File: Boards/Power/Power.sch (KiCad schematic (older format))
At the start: 105 parts, among them IC1 PIC32MM0064GPM048, K1 Relay(Mech/SSR), K2 Relay(Mech/SSR), K3 Relay(Mech/SSR), K4 Relay(Mech/SSR), K5 Relay(Mech/SSR), K6 Relay(Mech/SSR), K7 Relay(Mech/SSR), K8 Relay(Mech/SSR), P1 Stab and 1x3, P10 1x6 2.54 Pin Header, P11 Stacked USBA, P12 1x2 5.08, P13 1x2 5.08, P2 Stab and 1x3, P3 Stab and 1x3, P4 Stab and 1x3, P5 Stab and 1x3, P6 Stab and 1x3, P7 Stab and 1x3, P8 Stab and 1x3, Q1 NX7002AK, Q10 NX7002AK, Q11 NX7002AK, Q2 NX7002AK, Q3 NX7002AK, Q4 NX7002AK, Q5 NX7002AK, Q6 NX7002AK, Q7 NX7002AK, Q8 NX7002AK, Q9 NX7002AK, U1 ST485EC, U2 AP2114H, U3 LTV-826, U4 LTV-826, X1 8MHz

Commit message: Power bom is now controlled by schematic
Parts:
- added N1: Housing, symbol Mechanical:Housing
- added P11, P12, P13, P14, P15, P16, P17, P18: Current, Connector_PinSocket_2.54mm:PinSocket_1x03_P2.54mm_Vertical, symbol Connector_Generic:Conn_01x03
- C1, C2, C3, C4: symbol C_Small -> Power-rescue:C_Small; Comments (none) -> 0805, 50V, X7R, 10%; Digi-Key Part Number (none) -> 445-7534-1-ND; Manufacturer (none) -> TDK; Manufacturer Part Number (none) -> C2012X7R1H104K085AA; Type (none) -> Capacitor
- C5: symbol C -> Power-rescue:C_Small; Comments (none) -> 0805, 50V, X7R, 10%; Digi-Key Part Number (none) -> 445-7534-1-ND; Manufacturer (none) -> TDK; Manufacturer Part Number (none) -> C2012X7R1H104K085AA; Type (none) -> Capacitor
- C6, C7: symbol C_Small -> Power-rescue:C_Small; Comments (none) -> 0805, 10V, X7R, 10%; Digi-Key Part Number (none) -> 1276-2972-1-ND; Manufacturer (none) -> Samsung; Manufacturer Part Number (none) -> CL21B475KPFNNNE; Type (none) -> Capacitor
- C8: symbol C -> Power-rescue:C_Small; Comments (none) -> 1812, 400V, X7T, 20%; Digi-Key Part Number (none) -> 445-13461-1-ND; Manufacturer (none) -> TDK; Manufacturer Part Number (none) -> C4532X7T2W474M230KA; Type (none) -> Capacitor
- D1, D11, D13, D15, D3, D5, D7, D9: symbol LED_ALT -> Power-rescue:LED_ALT; Comments (none) -> 0805, 3.2V, 20mA; Digi-Key Part Number (none) -> 732-4982-1-ND; Manufacturer (none) -> Wurth; Manufacturer Part Number (none) -> 150080BS75000; Type (none) -> LED (BLUE)
- D10, D12, D14, D16, D2, D4, D6, D8: symbol DIODESCH -> Power-rescue:DIODESCH; Comments (none) -> DO-214AC; Digi-Key Part Number (none) -> 497-3755-1-ND; Manufacturer (none) -> STMicroelectronics; Manufacturer Part Number (none) -> STPS130A; Type (none) -> Schottky Diode
- D17: symbol TRI-LED -> GoodtimeDev:TRI-LED; Comments (none) -> 4-PLCC; Digi-Key Part Number (none) -> 492-2173-1-ND; Manufacturer (none) -> Bivar; Manufacturer Part Number (none) -> SMTL4-RGY; Type (none) -> LED (Red, Green, Yellow)
- D18, D19: symbol LED_ALT -> Power-rescue:LED_ALT; Comments (none) -> 0805, 2V, 20mA; Digi-Key Part Number (none) -> 475-1278-1-ND; Manufacturer (none) -> Osram; Manufacturer Part Number (none) -> LS R976-NR-1; Type (none) -> LED (RED)
- IC1: symbol PIC32MM0064GPM048_QFN -> GoodtimeDev:PIC32MM0064GPM048_QFN; Comments (none) -> 48-TQFP 7mm; Digi-Key Part Number (none) -> PIC32MM0064GPM048T-I/PTCT-ND; Manufacter Part Number PIC32MM0064GPM048T-I/PT -> (none); Manufacturer (none) -> Microchip; Manufacturer Part Number (none) -> PIC32MM0064GPM048T-I/PT; Type (none) -> Microcontroller
- K1, K2: symbol Relay(Mech/SSR) -> Power-rescue:Relay(Mech_SSR); Comments (none) -> -; Digi-Key Part Number (none) -> 255-3559-ND; Manufacturer (none) -> Panasonic; Manufacturer Part Number (none) -> ALQ305; Type (none) -> Mechanical Relay
- K3, K4, K5, K6, K7, K8: symbol Relay(Mech/SSR) -> Power-rescue:Relay(Mech_SSR); Comments (none) -> -; Digi-Key Part Number (none) -> -; Manufacturer (none) -> Mager; Manufacturer Part Number (none) -> GJ-5-L; Type (none) -> SSR Relay
- P1, P2, P3, P4, P5, P6, P7, P8: value Stab and 1x3 -> Output; symbol Conn_01x04 -> Connector_Generic:Conn_01x01; Comments (none) -> -; Digi-Key Part Number (none) -> A29937CT-ND; Manufacturer (none) -> TE; Manufacturer Part Number (none) -> 63823-1; Type (none) -> Stab
- P10: renamed from P11; value Stacked USBA -> AquaPicBus; symbol USB1.0_Stacked -> GoodtimeDev:USB1.0_Stacked; Comments (none) -> -; Digi-Key Part Number (none) -> 1175-1003-ND; Manufacturer (none) -> CNC Tech; Manufacturer Part Number (none) -> 1001-004-01010; Type (none) -> USB 1.1 Type A
- P19: renamed from P12; value 1x2 5.08 -> Mains; symbol Conn_01x02 -> Power-rescue:Conn_01x02; Comments (none) -> -; Digi-Key Part Number (none) -> ED2580-ND; Manufacturer (none) -> On Shore; Manufacturer Part Number (none) -> OSTTA024163; Type (none) -> 1x2 5.08 Screw Header
- P20: renamed from P13; value 1x2 5.08 -> Mains; symbol Conn_01x02 -> Power-rescue:Conn_01x02; Comments (none) -> -; Digi-Key Part Number (none) -> ED2580-ND; Manufacturer (none) -> On Shore; Manufacturer Part Number (none) -> OSTTA024163; Type (none) -> 1x2 5.08 Screw Header
- P9: renamed from P10; value 1x6 2.54 Pin Header -> ICSP; symbol Conn_01x06 -> Power-rescue:Conn_01x06; Comments (none) -> -; Digi-Key Part Number (none) -> A105161CT-ND; Manufacturer (none) -> TE; Manufacturer Part Number (none) -> A105161CT-ND; Type (none) -> 1x6 2.54 Male Pin Header
- Q1, Q10, Q11, Q2, Q3, Q4, Q5, Q6, Q7, Q8, Q9: symbol MOSFET_N_SMALL -> GoodtimeDev:MOSFET_N_SMALL; Comments (none) -> SOT-23-3; Digi-Key Part Number (none) -> 1727-1289-6-ND; Manufacturer (none) -> Nexperia; Manufacturer Part Number (none) -> NX7002AK,215; Type (none) -> N-Channel MOSFET
- R1, R10, R13, R16, R19, R22, R25, R4, R7: symbol R -> Power-rescue:R; Comments (none) -> 0805, 1/4W, 1%, Thin Film; Digi-Key Part Number (none) -> RNCP0805FTD1K00CT-ND; Manufacturer (none) -> Stackpole; Manufacturer Part Number (none) -> RNCP0805FTD1K00; Type (none) -> Resistor
- R11, R14, R17, R2, R20, R23, R26, R27, R39, R5, R8: symbol R -> Power-rescue:R; Comments (none) -> 0805, 1/4W, 1%, Thin Film; Digi-Key Part Number (none) -> RNCP0805FTD10K0CT-ND; Manufacturer (none) -> Stackpole; Manufacturer Part Number (none) -> RNCP0805FTD10K0; Type (none) -> Resistor
- R12, R15, R18, R21, R24, R3, R32, R33, R34, R35, R38, R6, R9: symbol R -> Power-rescue:R; Comments (none) -> 0805, 1/4W, 1%, Thin Film; Digi-Key Part Number (none) -> RNCP0805FTD150RCT-ND; Manufacturer (none) -> Stackpole; Manufacturer Part Number (none) -> RNCP0805FTD150R; Type (none) -> Resistor
- R28, R29, R30, R31: symbol R -> Power-rescue:R; Comments (none) -> 0805, 1/4W, 1%, Thin Film; Digi-Key Part Number (none) -> RNCP0805FTD4K99CT-ND; Manufacturer (none) -> Stackpole; Manufacturer Part Number (none) -> RNCP0805FTD4K99; Type (none) -> Resistor
- R36: symbol R -> Power-rescue:R; Comments (none) -> 2010, 3/4W, 5%, Thick Film; Digi-Key Part Number (none) -> P1.0MWCT-ND; Manufacturer (none) -> Panasonic; Manufacturer Part Number (none) -> P1.0MW; Type (none) -> Resistor
- R37: symbol R -> Power-rescue:R; Comments (none) -> 2512, 1W, 1%, Thick Film; Digi-Key Part Number (none) -> 541-1.00KAFCT-ND; Manufacturer (none) -> Vishay Dale; Manufacturer Part Number (none) -> CRCW25121K00FKEG; Type (none) -> Resistor
- R40, R41: symbol R -> Power-rescue:R; Comments (none) -> 2512, 1W, 1%, Thick Film; Digi-Key Part Number (none) -> RHM13.7KBBCT-ND; Manufacturer (none) -> Rohm; Manufacturer Part Number (none) -> MCR100JZHF1372; Type (none) -> Resistor
- U1: symbol SN75176B -> GoodtimeDev:SN75176B; Comments (none) -> 8-SOIC 3.9mm; Digi-Key Part Number (none) -> 497-3735-1-ND; Manufacturer (none) -> STMicro; Manufacturer Part Number (none) -> ST485ECDR; Type (none) -> RS485 Transceiver
- U2: symbol AP1117-33 -> Power-rescue:AP1117-33; Comments (none) -> SOT-223; Digi-Key Part Number (none) -> AP2114HA-2.5TRG1DICT-ND; Manufacturer (none) -> Diodes; Manufacturer Part Number (none) -> AP2114HA-2.5TRG1; Type (none) -> Linear Regulator
- U3, U4: symbol LTV-826 -> GoodtimeDev:LTV-826; Comments (none) -> 8-SMD; Digi-Key Part Number (none) -> 160-1363-5-ND; Manufacturer (none) -> Lite-On; Manufacturer Part Number (none) -> LTV-826S; Type (none) -> Dual Opto-Isolator
- X1: symbol RESONATOR -> GoodtimeDev:RESONATOR; Comments (none) -> 3-SMD, Non-Standard; Digi-Key Part Number (none) -> 490-1195-1-ND; Manufacturer (none) -> Murata; Manufacturer Part Number (none) -> CSTCE8M00G55-R0; Type (none) -> Resonator
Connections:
- net +5V: now also P11.1 (Pin_1), P12.1 (Pin_1), P13.1 (Pin_1), P14.1 (Pin_1), P15.1 (Pin_1), P16.1 (Pin_1), P17.1 (Pin_1), P18.1 (Pin_1); no longer P1.2 (Pin_2), P2.2 (Pin_2), P3.2 (Pin_2), P4.2 (Pin_2), P5.2 (Pin_2), P6.2 (Pin_2), P7.2 (Pin_2), P8.2 (Pin_2)
- net CURRENT_1: now also P11.2 (Pin_2); no longer P1.3 (Pin_3)
- net CURRENT_2: now also P12.2 (Pin_2); no longer P2.3 (Pin_3)
- net CURRENT_3: now also P13.2 (Pin_2); no longer P3.3 (Pin_3)
- net CURRENT_4: now also P14.2 (Pin_2); no longer P4.3 (Pin_3)
- net CURRENT_5: now also P15.2 (Pin_2); no longer P5.3 (Pin_3)
- net CURRENT_6: now also P16.2 (Pin_2); no longer P6.3 (Pin_3)
- net CURRENT_7: now also P17.2 (Pin_2); no longer P7.3 (Pin_3)
- net CURRENT_8: now also P18.2 (Pin_2); no longer P8.3 (Pin_3)
- net GND: now also P11.3 (Pin_3), P12.3 (Pin_3), P13.3 (Pin_3), P14.3 (Pin_3), P15.3 (Pin_3), P16.3 (Pin_3), P17.3 (Pin_3), P18.3 (Pin_3); no longer P1.4 (Pin_4), P2.4 (Pin_4), P3.4 (Pin_4), P4.4 (Pin_4), P5.4 (Pin_4), P6.4 (Pin_4), P7.4 (Pin_4), P8.4 (Pin_4)

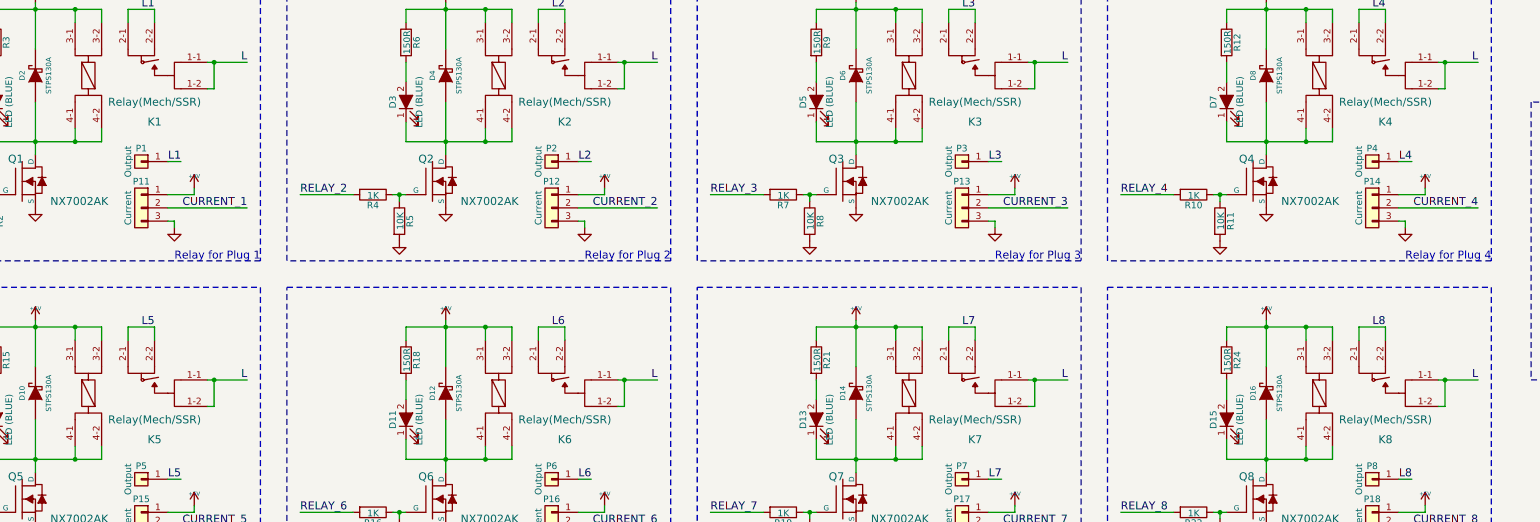
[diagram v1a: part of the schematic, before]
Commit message: generated BOMs
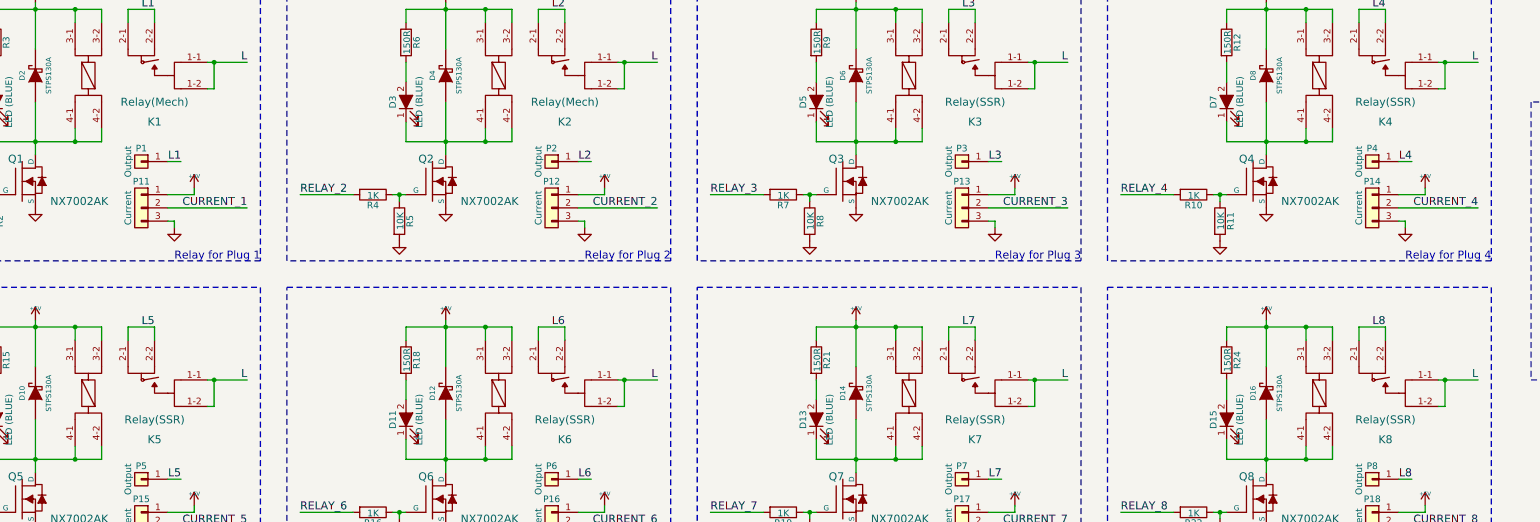
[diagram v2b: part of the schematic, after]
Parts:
- K1, K2: value Relay(Mech/SSR) -> Relay(Mech)
- K3, K4, K5, K6, K7, K8: value Relay(Mech/SSR) -> Relay(SSR)
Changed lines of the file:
@@
 P 2500 1500
 F 0 "K1" H 2800 1150 60  0000 C CNN
-F 1 "Relay(Mech/SSR)" H 2800 1300 60  0000 C CNN
+F 1 "Relay(Mech)" H 2800 1300 60  0000 C CNN
 F 2 "MyFootPrints:Relay-Mech-SSR" H 3800 500 60  0001 C CNN
 F 3 "" H 3800 500 60  0000 C CNN
@@
 P 5600 1500
 F 0 "K2" H 5900 1150 60  0000 C CNN
-F 1 "Relay(Mech/SSR)" H 5900 1300 60  0000 C CNN
+F 1 "Relay(Mech)" H 5900 1300 60  0000 C CNN
 F 2 "MyFootPrints:Relay-Mech-SSR" H 6900 500 60  0001 C CNN
 F 3 "" H 6900 500 60  0000 C CNN
@@
 P 8700 1500
 F 0 "K3" H 9000 1150 60  0000 C CNN
-F 1 "Relay(Mech/SSR)" H 9000 1300 60  0000 C CNN
+F 1 "Relay(SSR)" H 9000 1300 60  0000 C CNN
 F 2 "MyFootPrints:Relay-Mech-SSR" H 10000 500 60  0001 C CNN
 F 3 "" H 10000 500 60  0000 C CNN
@@
 P 11800 1500
 F 0 "K4" H 12100 1150 60  0000 C CNN
-F 1 "Relay(Mech/SSR)" H 12100 1300 60  0000 C CNN
+F 1 "Relay(SSR)" H 12100 1300 60  0000 C CNN
 F 2 "MyFootPrints:Relay-Mech-SSR" H 13100 500 60  0001 C CNN
 F 3 "" H 13100 500 60  0000 C CNN
@@
 P 2500 3900
 F 0 "K5" H 2800 3550 60  0000 C CNN
-F 1 "Relay(Mech/SSR)" H 2800 3700 60  0000 C CNN
+F 1 "Relay(SSR)" H 2800 3700 60  0000 C CNN
 F 2 "MyFootPrints:Relay-Mech-SSR" H 3800 2900 60  0001 C CNN
 F 3 "" H 3800 2900 60  0000 C CNN
@@
 P 5600 3900
 F 0 "K6" H 5900 3550 60  0000 C CNN
-F 1 "Relay(Mech/SSR)" H 5900 3700 60  0000 C CNN
+F 1 "Relay(SSR)" H 5900 3700 60  0000 C CNN
 F 2 "MyFootPrints:Relay-Mech-SSR" H 6900 2900 60  0001 C CNN
 F 3 "" H 6900 2900 60  0000 C CNN
@@
 P 8700 3900
 F 0 "K7" H 9000 3550 60  0000 C CNN
-F 1 "Relay(Mech/SSR)" H 9000 3700 60  0000 C CNN
+F 1 "Relay(SSR)" H 9000 3700 60  0000 C CNN
 F 2 "MyFootPrints:Relay-Mech-SSR" H 10000 2900 60  0001 C CNN
 F 3 "" H 10000 2900 60  0000 C CNN
@@
 P 11800 3900
 F 0 "K8" H 12100 3550 60  0000 C CNN
-F 1 "Relay(Mech/SSR)" H 12100 3700 60  0000 C CNN
+F 1 "Relay(SSR)" H 12100 3700 60  0000 C CNN
 F 2 "MyFootPrints:Relay-Mech-SSR" H 13100 2900 60  0001 C CNN
 F 3 "" H 13100 2900 60  0000 C CNN
